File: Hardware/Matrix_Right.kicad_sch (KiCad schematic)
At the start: 136 parts, among them SW37 PG1350, SW38 PG1350, SW39 PG1350, SW40 PG1350, SW41 PG1350, SW42 PG1350, SW43 PG1350, SW44 PG1350, SW45 PG1350, SW46 PG1350, SW47 PG1350, SW48 PG1350, SW49 PG1350, SW50 PG1350, SW51 PG1350, SW52 PG1350, SW53 PG1350, SW54 PG1350, SW55 PG1350, SW56 PG1350, SW57 PG1350, SW58 PG1350, SW59 PG1350, SW60 PG1350, SW61 PG1350, SW62 PG1350, SW63 PG1350, SW64 PG1350, SW65 PG1350, SW66 PG1350, SW67 PG1350, SW68 PG1350, SW69 PG1350, SW70 ENCODER

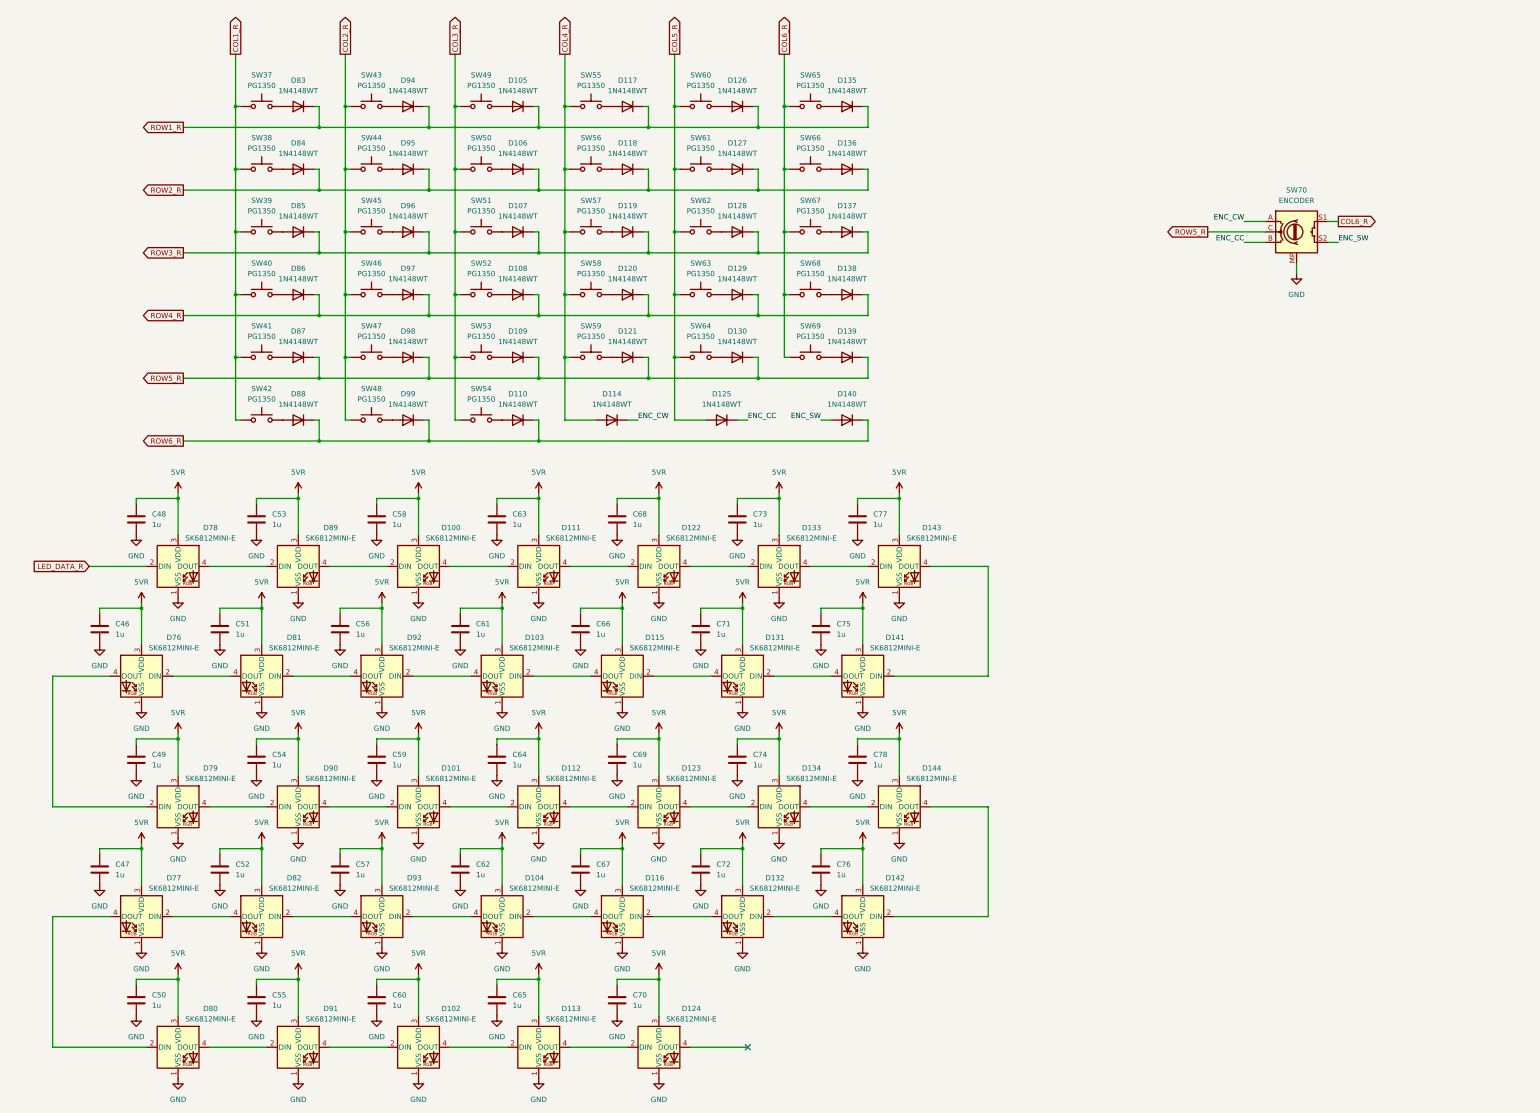
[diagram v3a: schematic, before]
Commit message: Pin adjustment
Adjusted the pins for the encoders and other.
Now the battery measuring pin connected to an internal ADC on the XIAO nRF52840 also serves to read the rotation of the encoders.
Attention should be put as how to implement the BAT voltage measuring to check if the encoder is turning at the same time.
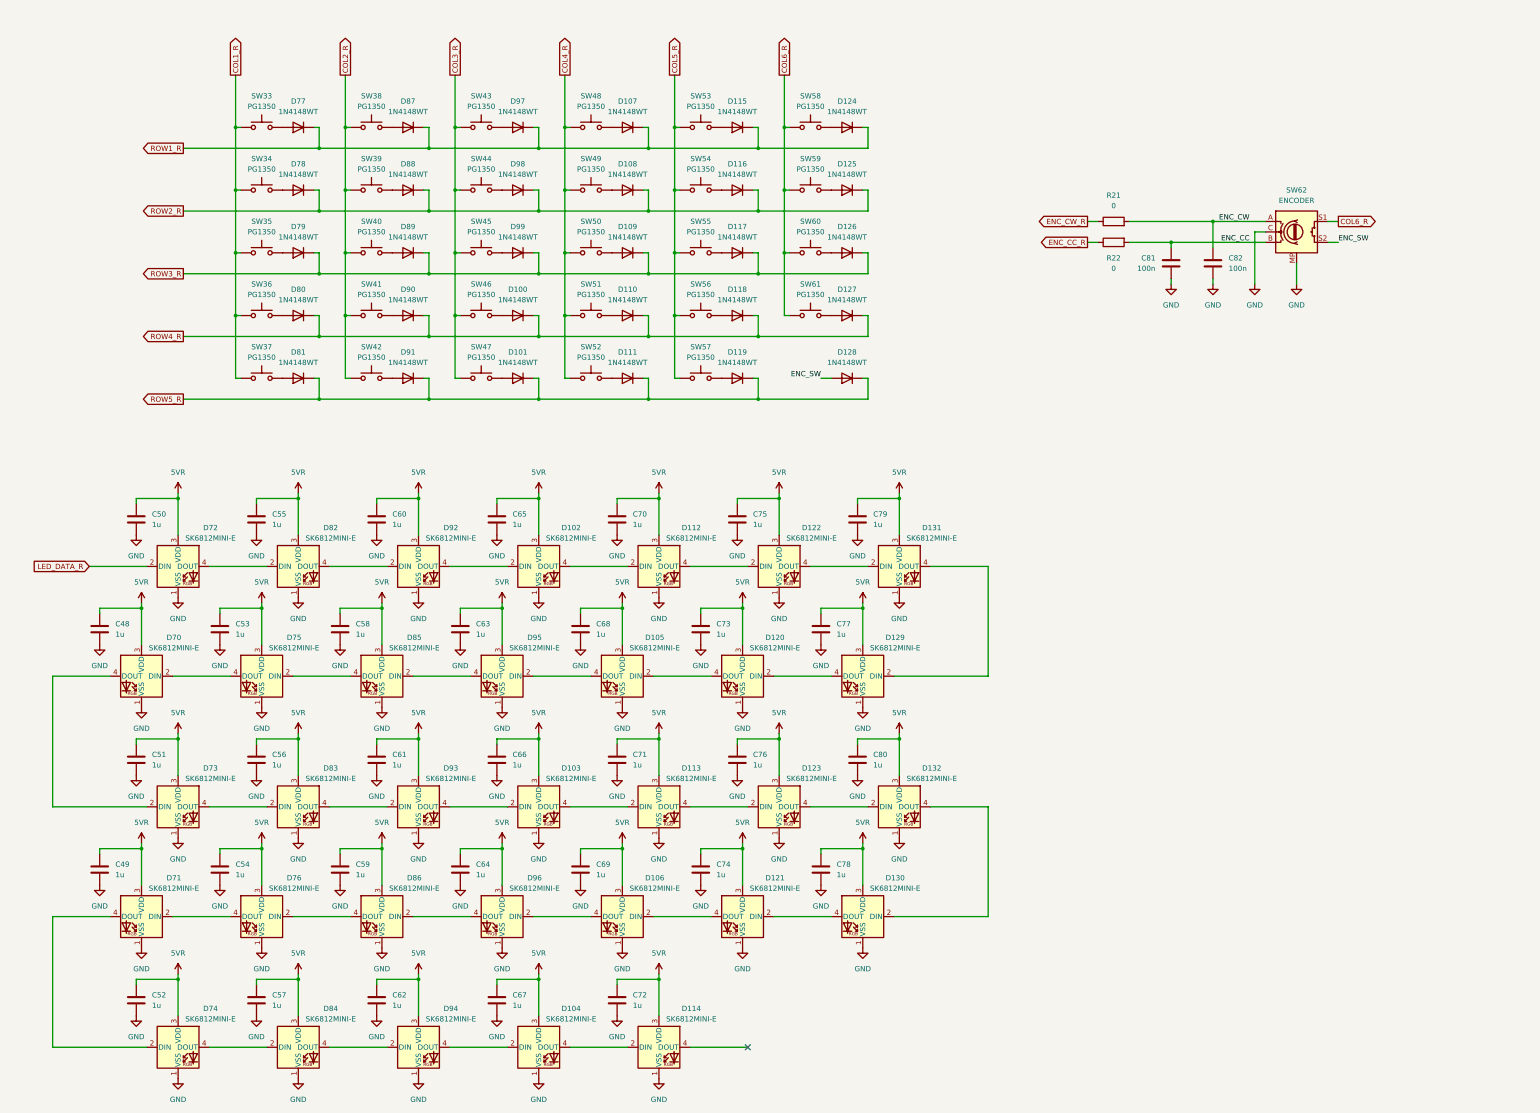
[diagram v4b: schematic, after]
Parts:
- removed D110, D114, D125, D140, D88, D99: 1N4148WT, Diode_SMD:D_SOD-523, symbol Diode:1N4148WT
- removed SW42, SW48, SW54, SW69: PG1350, Custom_Parts:PG1350_1.00u_PCB, symbol Switch:SW_Push
- added C81, C82: 100n, Capacitor_SMD:C_0603_1608Metric, symbol Device:C
- added R21, R22: 0, Resistor_SMD:R_0603_1608Metric, symbol Device:R
- renumbered C46 to C48, C47 to C49, C48 to C50, C49 to C51, C50 to C52, C51 to C53, C52 to C54, C53 to C55, C54 to C56, C55 to C57, C56 to C58, C57 to C59, C58 to C60, C59 to C61, C60 to C62, C61 to C63, C62 to C64, C63 to C65, C64 to C66, C65 to C67, C66 to C68, C67 to C69, C68 to C70, C69 to C71, C70 to C72, C71 to C73, C72 to C74, C73 to C75, C74 to C76, C75 to C77, C76 to C78, C77 to C79, C78 to C80, D108 to D100, D109 to D101, D111 to D102, D112 to D103, D113 to D104, D115 to D105, D116 to D106, D117 to D107, D118 to D108, D119 to D109, D120 to D110, D121 to D111, D122 to D112, D123 to D113, D124 to D114, D126 to D115, D127 to D116, D128 to D117, D129 to D118, D130 to D119, D131 to D120, D132 to D121, D133 to D122, D134 to D123, D135 to D124, D136 to D125, D137 to D126, D138 to D127, D139 to D128, D141 to D129, D142 to D130, D143 to D131, D144 to D132, D76 to D70, D77 to D71, D78 to D72, D79 to D73, D80 to D74, D81 to D75, D82 to D76, D83 to D77, D84 to D78, D85 to D79, D86 to D80, D87 to D81, D89 to D82, D90 to D83, D91 to D84, D92 to D85, D93 to D86, D94 to D87, D95 to D88, D96 to D89, D97 to D90, D98 to D91, D100 to D92, D101 to D93, D102 to D94, D103 to D95, D104 to D96, D105 to D97, D106 to D98, D107 to D99, SW37 to SW33, SW38 to SW34, SW39 to SW35, SW40 to SW36, SW41 to SW37, SW43 to SW38, SW44 to SW39, SW45 to SW40, SW46 to SW41, SW47 to SW42, SW49 to SW43, SW50 to SW44, SW51 to SW45, SW52 to SW46, SW53 to SW47, SW55 to SW48, SW56 to SW49, SW57 to SW50, SW58 to SW51, SW59 to SW52, SW60 to SW53, SW61 to SW54, SW62 to SW55, SW63 to SW56, SW64 to SW57, SW65 to SW58, SW66 to SW59, SW67 to SW60, SW68 to SW61, SW70 to SW62
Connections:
- net ENC_CC: now also C81.1, R22.2
- net ENC_CW: now also C82.1, R21.2
- net ENC_SW: now also D128.2 (A)
- net GND: now also SW62.C, C81.2, C82.2
- net ROW5_R: no longer SW62.C
- new net ENC_CC_R: R22.1
- new net ENC_CW_R: R21.1
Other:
- moved on the sheet: D100, D101, D107, D108, D109, D110, D111, D115, D116, D117, D118, D119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

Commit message: Layout coordination
Coordinated the layout with the schematic.
Finished the initial switch layout.
Need to decide on a complete layout for the keyboard and assign the auxiliary keys.
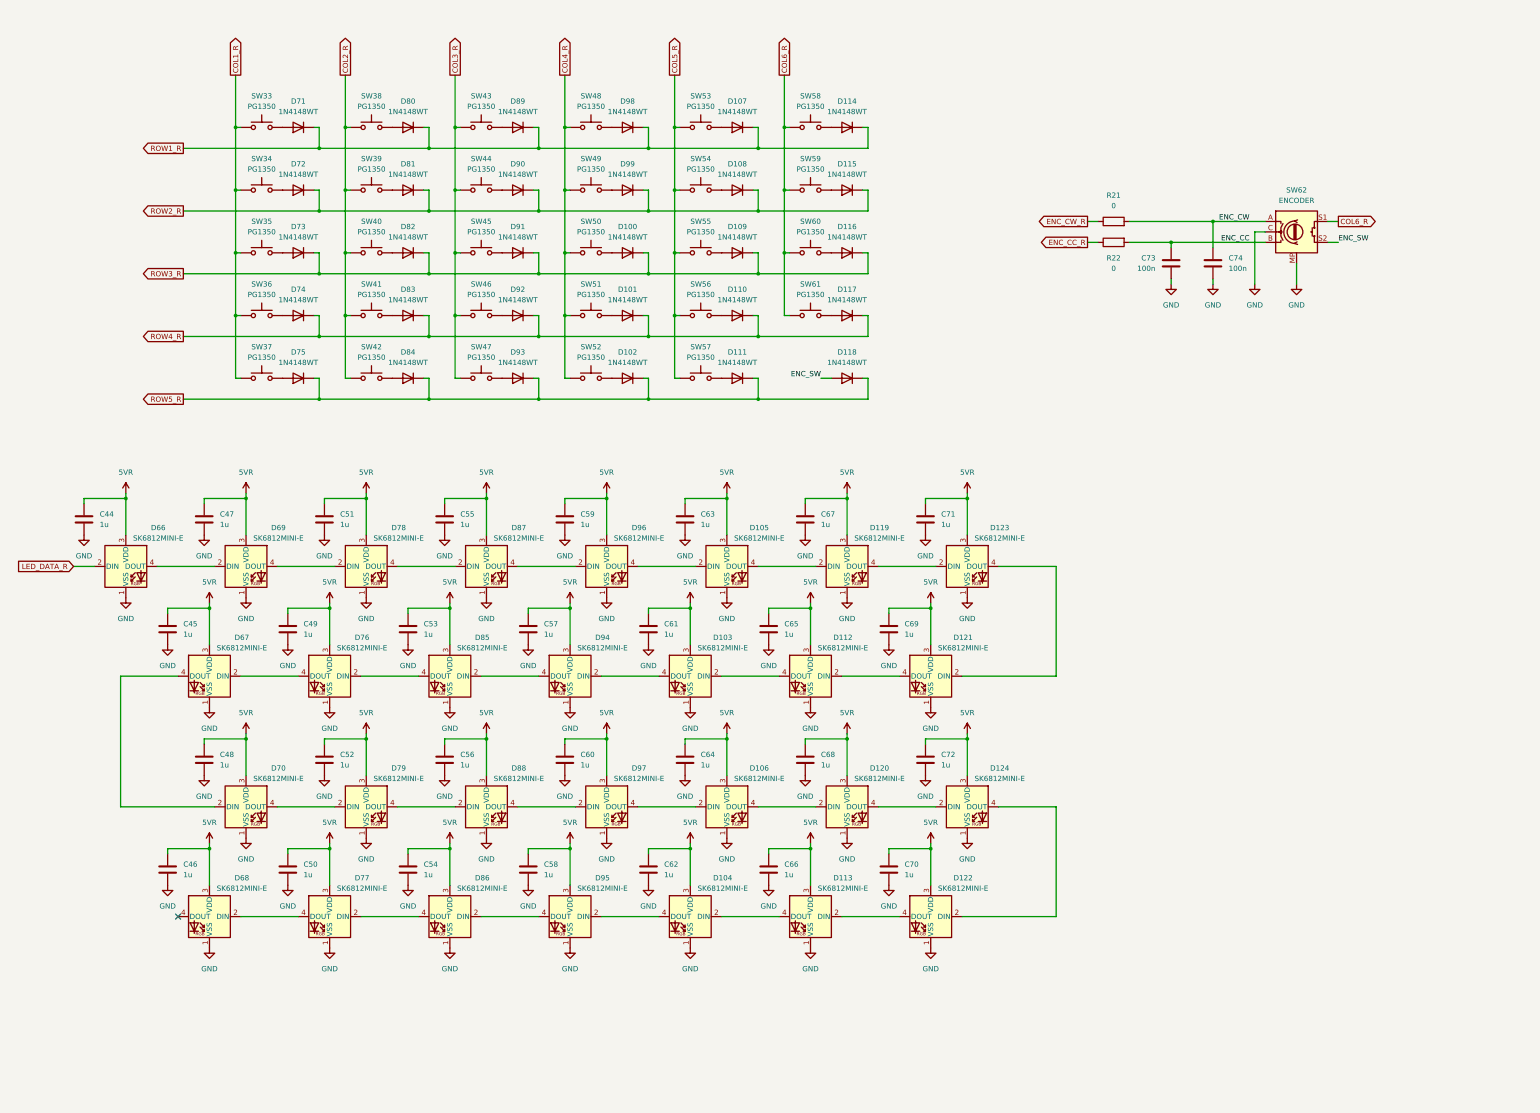
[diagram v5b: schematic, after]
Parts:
- removed C52, C57, C62, C67, C72: 1u, Capacitor_SMD:C_0603_1608Metric, symbol Device:C
- removed D104, D114, D74, D84, D94: SK6812MINI-E, Custom_Parts:LED_SK6812MINI-E_3.2x2.8mm_P1.5mm_ReverseMount, symbol LED:SK6812MINI-E
- added C44: 1u, Capacitor_SMD:C_0603_1608Metric, symbol Device:C
- added D66: SK6812MINI-E, Custom_Parts:LED_SK6812MINI-E_3.2x2.8mm_P1.5mm_ReverseMount, symbol LED:SK6812MINI-E
- renumbered C48 to C45, C49 to C46, C50 to C47, C51 to C48, C53 to C49, C54 to C50, C55 to C51, C56 to C52, C58 to C53, C59 to C54, C60 to C55, C61 to C56, C63 to C57, C64 to C58, C65 to C59, C66 to C60, C68 to C61, C69 to C62, C70 to C63, C71 to C64, C73 to C65, C74 to C66, C75 to C67, C76 to C68, C77 to C69, C78 to C70, C79 to C71, C80 to C72, C81 to C73, C82 to C74, D109 to D100, D110 to D101, D111 to D102, D105 to D103, D106 to D104, D112 to D105, D113 to D106, D115 to D107, D116 to D108, D117 to D109, D118 to D110, D119 to D111, D120 to D112, D121 to D113, D124 to D114, D125 to D115, D126 to D116, D127 to D117, D128 to D118, D122 to D119, D123 to D120, D129 to D121, D130 to D122, D131 to D123, D132 to D124, D70 to D67, D71 to D68, D72 to D69, D73 to D70, D77 to D71, D78 to D72, D79 to D73, D80 to D74, D81 to D75, D75 to D76, D76 to D77, D82 to D78, D83 to D79, D87 to D80, D88 to D81, D89 to D82, D90 to D83, D91 to D84, D92 to D87, D93 to D88, D97 to D89, D98 to D90, D99 to D91, D100 to D92, D101 to D93, D95 to D94, D96 to D95, D102 to D96, D103 to D97, D107 to D98, D108 to D99
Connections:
- net 5VR: now also C44.1, D66.3 (VDD)
- net GND: now also C44.2, D66.1 (VSS)
- net LED_DATA_R: now also D66.2 (DIN); no longer D69.2 (DIN)
- new net: D66.4 (DOUT), D69.2 (DIN)
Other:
- moved on the sheet: C45, C46, C47, C48, C49, C50, C51, C52, C53, C54, C55, C56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

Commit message: Key matrix and edges
Defined the key matrix locations and the board edges.
Next step: start routing and verify the buck converter layout.
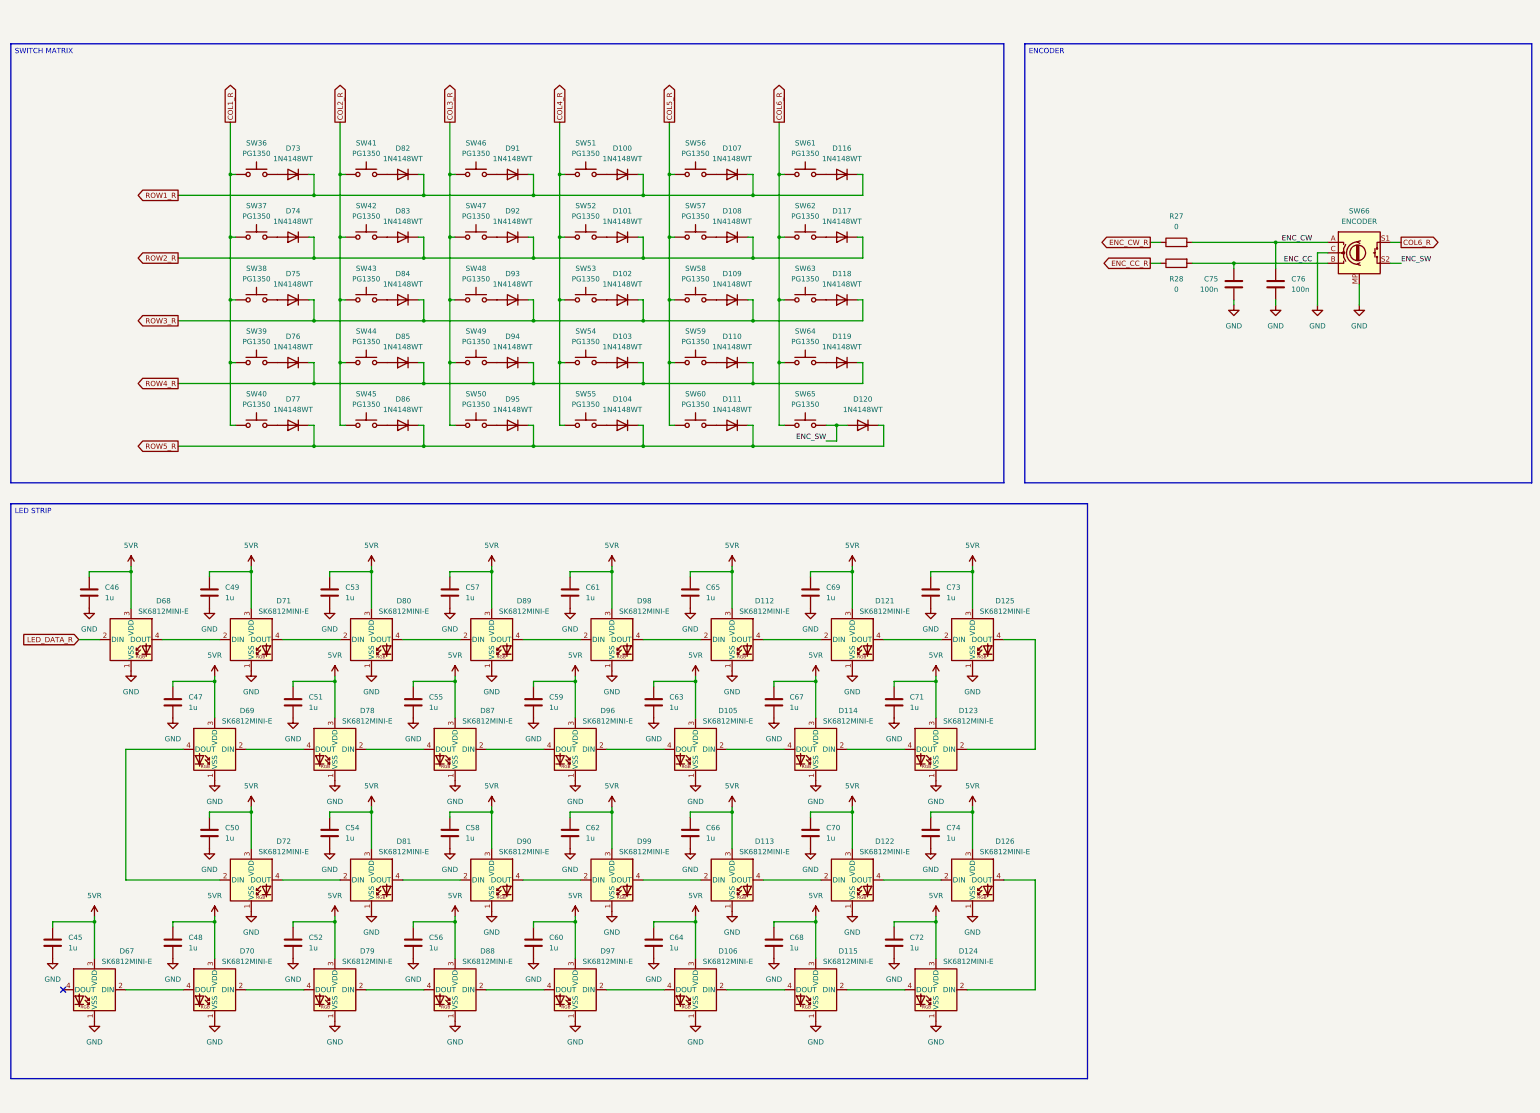
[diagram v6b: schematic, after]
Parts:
- removed C44: 1u, Capacitor_SMD:C_0603_1608Metric, symbol Device:C
- removed D103, D104, D119, D120, D66, D76, D77, D85, D86, D94, D95: SK6812MINI-E, Custom_Parts:LED_SK6812MINI-E_3.2x2.8mm_P1.5mm_ReverseMount, symbol LED:SK6812MINI-E
- removed D114, D115, D71, D72, D80, D81, D89, D90, D98, D99: 1N4148WT, Diode_SMD:D_SOD-523, symbol Diode:1N4148WT
- removed R21, R22: 0, Resistor_SMD:R_0603_1608Metric, symbol Device:R
- removed SW33, SW34, SW35: PG1350, Custom_Parts:PG1350_1.00u_PCB, symbol Switch:SW_Push
- removed SW62: ENCODER, Custom_Parts:ALPS_EC11J_ENCODER, symbol Device:RotaryEncoder_Switch_MP
- added C75, C76: 100n, Capacitor_SMD:C_0603_1608Metric, symbol Device:C
- added D103, D104, D119, D120, D76, D77, D85, D86, D94, D95: 1N4148WT, Diode_SMD:D_SOD-523, symbol Diode:1N4148WT
- added D114, D115, D125, D126, D71, D72, D80, D81, D89, D90, D98, D99: SK6812MINI-E, Custom_Parts:LED_SK6812MINI-E_3.2x2.8mm_P1.5mm_ReverseMount, symbol LED:SK6812MINI-E
- added R27, R28: 0, Resistor_SMD:R_0603_1608Metric, symbol Device:R
- added SW62, SW63, SW64, SW65: PG1350, Custom_Parts:PG1350_1.00u_PCB, symbol Switch:SW_Push
- added SW66: ENCODER, Custom_Parts:ALPS_EC11J_ENCODER, symbol Device:RotaryEncoder_Switch_MP
- C73, C74: value 100n -> 1u; JLC Part C14663 -> C15849; Manufacturer Part CC0603KRX7R9BB104 -> CL10A105KB8NNNC; now in the parts list
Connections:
- net 5VR: now also C73.1, C74.1, D114.3 (VDD), D115.3 (VDD), D125.3 (VDD), D126.3 (VDD), D71.3 (VDD), D72.3 (VDD), D80.3 (VDD), D81.3 (VDD), D89.3 (VDD), D90.3 (VDD), D98.3 (VDD), D99.3 (VDD)
- net COL1_R: now also SW38.1, SW39.1, SW40.1
- net COL2_R: now also SW43.1, SW44.1, SW45.1; no longer SW38.1, SW39.1, SW40.1
- net COL3_R: now also SW48.1, SW49.1, SW50.1; no longer SW43.1, SW44.1, SW45.1
- net COL4_R: now also SW53.1, SW54.1, SW55.1; no longer SW48.1, SW49.1, SW50.1
- net COL5_R: now also SW58.1, SW59.1, SW60.1; no longer SW53.1, SW54.1, SW55.1
- net COL6_R: now also SW62.1, SW63.1, SW64.1, SW65.1, SW66.S1; no longer SW58.1, SW59.1, SW60.1
- net ENC_CC: now also C75.1, R28.2, SW66.B; no longer C73.1
- net ENC_CC_R: now also R28.1
- net ENC_CW: now also C76.1, R27.2, SW66.A; no longer C74.1
- net ENC_CW_R: now also R27.1
- net ENC_SW: now also D120.2 (A), SW65.2, SW66.S2; no longer D118.2 (A)
- net GND: now also C75.2, C76.2, D114.1 (VSS), D115.1 (VSS), D125.1 (VSS), D126.1 (VSS), D71.1 (VSS), D72.1 (VSS), D80.1 (VSS), D81.1 (VSS), D89.1 (VSS), D90.1 (VSS), D98.1 (VSS), D99.1 (VSS), SW66.C, SW66.MP
- net LED_DATA_R: now also D68.2 (DIN)
- net ROW1_R: now also D100.1 (K), D116.1 (K), D73.1 (K), D82.1 (K), D91.1 (K)
- net ROW2_R: now also D101.1 (K), D117.1 (K), D74.1 (K), D83.1 (K), D92.1 (K)
- net ROW3_R: now also D102.1 (K), D118.1 (K), D75.1 (K), D84.1 (K), D93.1 (K); no longer D100.1 (K), D116.1 (K), D73.1 (K), D82.1 (K), D91.1 (K)
- net ROW4_R: now also D103.1 (K), D119.1 (K), D76.1 (K), D85.1 (K), D94.1 (K); no longer D101.1 (K), D117.1 (K), D74.1 (K), D83.1 (K), D92.1 (K)
- net ROW5_R: now also D104.1 (K), D120.1 (K), D77.1 (K), D86.1 (K), D95.1 (K); no longer D102.1 (K), D118.1 (K), D75.1 (K), D84.1 (K), D93.1 (K)
- net at SW53.2: now also D102.2 (A); no longer D107.2 (A)
- net at D70.4 (DOUT): now also D67.2 (DIN); no longer D79.2 (DIN)
- net at D79.4 (DOUT): now also D70.2 (DIN); no longer D88.2 (DIN)
- net at SW59.2: now also D110.2 (A)
- net at D68.4 (DOUT): now also D71.2 (DIN)
- net at D100.2 (A): now also SW51.2; no longer SW50.2
- net at D82.2 (A): now also SW41.2; no longer SW40.2
- net at D97.2 (DIN): now also D106.4 (DOUT); no longer D88.4 (DOUT)
- net at D97.4 (DOUT): now also D88.2 (DIN); no longer D106.2 (DIN)
- net at D124.2 (DIN): now also D126.4 (DOUT)
- net at D124.4 (DOUT): now also D115.2 (DIN); no longer D122.2 (DIN)
- net at D84.2 (A): now also SW43.2; no longer SW42.2
- net at D117.2 (A): now also SW62.2; no longer SW61.2
- net at SW48.2: now also D93.2 (A)
- net at SW46.2: now also D91.2 (A); no longer D92.2 (A)
- net at D105.2 (DIN): now also D114.4 (DOUT); no longer D96.4 (DOUT)
- net at D105.4 (DOUT): now also D96.2 (DIN)
- net at SW44.2: now also D85.2 (A)
- net at SW58.2: now also D109.2 (A)
- net at D83.2 (A): now also SW42.2; no longer SW41.2
- net at D74.2 (A): now also SW37.2; no longer SW36.2
- net at SW45.2: now also D86.2 (A); no longer D91.2 (A)
- net at D78.4 (DOUT): now also D69.2 (DIN); no longer D87.2 (DIN)
- net at D87.4 (DOUT): now also D78.2 (DIN); no longer D96.2 (DIN)
- net at SW38.2: now also D75.2 (A)
- net at SW56.2: now also D107.2 (A); no longer D110.2 (A)
- net at D112.2 (DIN): now also D98.4 (DOUT); no longer D121.4 (DOUT)
- net at D112.4 (DOUT): now also D121.2 (DIN)
- net at D123.2 (DIN): now also D125.4 (DOUT)
- net at D73.2 (A): now also SW36.2
- net at SW55.2: now also D104.2 (A); no longer D109.2 (A)
- net at D113.2 (DIN): now also D99.4 (DOUT); no longer D122.4 (DOUT)
- net at D113.4 (DOUT): now also D122.2 (DIN)
- net at D101.2 (A): now also SW52.2; no longer SW51.2
- net at SW49.2: now also D94.2 (A)
- net at SW60.2: now also D111.2 (A); no longer D116.2 (A)
- net at SW54.2: now also D103.2 (A); no longer D108.2 (A)
- net at SW39.2: now also D76.2 (A)
- net at D67.4 (DOUT): no longer D70.2 (DIN)
- net at SW57.2: now also D108.2 (A); no longer D111.2 (A)
- net at SW47.2: now also D92.2 (A); no longer D93.2 (A)
- net at D69.4 (DOUT): now also D72.2 (DIN); no longer D78.2 (DIN)
- net at D123.4 (DOUT): now also D114.2 (DIN); no longer D121.2 (DIN)
- new net: D72.4 (DOUT), D81.2 (DIN)
- new net: D81.4 (DOUT), D90.2 (DIN)
- new net: D71.4 (DOUT), D80.2 (DIN)
- new net: D80.4 (DOUT), D89.2 (DIN)
- new net: D89.4 (DOUT), D98.2 (DIN)
- new net: D90.4 (DOUT), D99.2 (DIN)
- new net: D118.2 (A), SW63.2
- new net: D119.2 (A), SW64.2
- new net: D87.2 (DIN), D96.4 (DOUT)
- new net: D95.2 (A), SW50.2
- new net: D77.2 (A), SW40.2
- new net: D121.4 (DOUT), D125.2 (DIN)
- new net: D79.2 (DIN), D88.4 (DOUT)
- new net: D106.2 (DIN), D115.4 (DOUT)
- new net: D116.2 (A), SW61.2
- new net: D122.4 (DOUT), D126.2 (DIN)
